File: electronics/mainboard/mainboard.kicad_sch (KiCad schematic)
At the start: 2 parts, among them J1 Conn_02x03_Row_Letter_First

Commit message: add terminals
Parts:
- removed J1: Conn_02x03_Row_Letter_First, symbol Connector_Generic:Conn_02x03_Row_Letter_First
- added J1, J2: Conn_01x09, Wuerth:691247510009, symbol Connector_Generic:Conn_01x09
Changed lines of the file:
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@@
     (pin "VIN")
   )
-  (symbol (lib_id "Connector_Generic:Conn_02x03_Row_Letter_First") (at 100.33 50.8 0) (unit 1)
+  (symbol (lib_id "Connector_Generic:Conn_01x09") (at 71.12 50.8 0) (unit 1)
     (in_bom yes) (on_board yes) (fields_autoplaced)
-    (property "Reference" "J1" (id 0) (at 101.6 41.91 0))
-    (property "Value" "Conn_02x03_Row_Letter_First" (id 1) (at 101.6 44.45 0))
-    (property "Footprint" "" (id 2) (at 100.33 50.8 0)
+    (property "Reference" "J1" (id 0) (at 73.66 49.5299 0)
+      (effects (font (size 1.27 1.27)) (justify left))
+    )
+    (property "Value" "Conn_01x09" (id 1) (at 73.66 52.0699 0)
+      (effects (font (size 1.27 1.27)) (justify left) hide)
+    )
+    (property "Footprint" "Wuerth:691247510009" (id 2) (at 71.12 50.8 0)
       (effects (font (size 1.27 1.27)) hide)
     )
-    (property "Datasheet" "~" (id 3) (at 100.33 50.8 0)
+    (property "Datasheet" "~" (id 3) (at 71.12 50.8 0)
       (effects (font (size 1.27 1.27)) hide)
     )
-    (pin "a1")
-    (pin "a2")
-    (pin "a3")
-    (pin "b1")
-    (pin "b2")
-    (pin "b3")
+    (pin "1")
+    (pin "2")
+    (pin "3")
+    (pin "4")
+    (pin "5")
+    (pin "6")
+    (pin "7")
+    (pin "8")
+    (pin "9")
+  )
+  (symbol (lib_id "Connector_Generic:Conn_01x09") (at 96.52 50.8 0) (unit 1)
+    (in_bom yes) (on_board yes) (fields_autoplaced)
+    (property "Reference" "J2" (id 0) (at 99.06 49.5299 0)
+      (effects (font (size 1.27 1.27)) (justify left))
+    )
+    (property "Value" "Conn_01x09" (id 1) (at 99.06 52.0699 0)
+      (effects (font (size 1.27 1.27)) (justify left) hide)
+    )
+    (property "Footprint" "Wuerth:691247510009" (id 2) (at 96.52 50.8 0)
+      (effects (font (size 1.27 1.27)) hide)
+    )
+    (property "Datasheet" "~" (id 3) (at 96.52 50.8 0)
+      (effects (font (size 1.27 1.27)) hide)
+    )
+    (pin "1")
+    (pin "2")
+    (pin "3")
+    (pin "4")
+    (pin "5")
+    (pin "6")
+    (pin "7")
+    (pin "8")
+    (pin "9")
   )
   (sheet_instances
@@
   )
   (symbol_instances
-    (path "/b954af0c-d64a-4750-8531-d504b8da04e4"
-      (reference "J1") (unit 1) (value "Conn_02x03_Row_Letter_First") (footprint "")
+    (path "/348d43a5-aba5-4633-9cec-22de12d03f26"
+      (reference "J1") (unit 1) (value "Conn_01x09") (footprint "Wuerth:691247510009")
+    )
+    (path "/adc82490-344e-430a-b2ea-febe9c558b97"
+      (reference "J2") (unit 1) (value "Conn_01x09") (footprint "Wuerth:691247510009")
     )
     (path "/135780b7-b5c1-44d5-9cc5-e01fba31ba00"

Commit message: place parts
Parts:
- added J3, J4, J5, J6, J7, J8, J9: Conn_01x09, Wuerth:691247510009, symbol Connector_Generic:Conn_01x09
- added J99: Conn_01x08, Connector_PinHeader_2.54mm:PinHeader_1x08_P2.54mm_Vertical_SMD_Pin1Right, symbol Connector_Generic:Conn_01x08
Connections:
- net at XA1.A0: now also J99.1 (Pin_1)
- net at XA1.A1: now also J99.2 (Pin_2)
- net at XA1.A2: now also J99.3 (Pin_3)
- net at XA1.A3: now also J99.4 (Pin_4)
- net at XA1.A4: now also J99.5 (Pin_5)
- net at XA1.A5: now also J99.6 (Pin_6)
- net at XA1.A6: now also J99.7 (Pin_7)
- net at XA1.A7: now also J99.8 (Pin_8)
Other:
- moved on the sheet: J1, J2

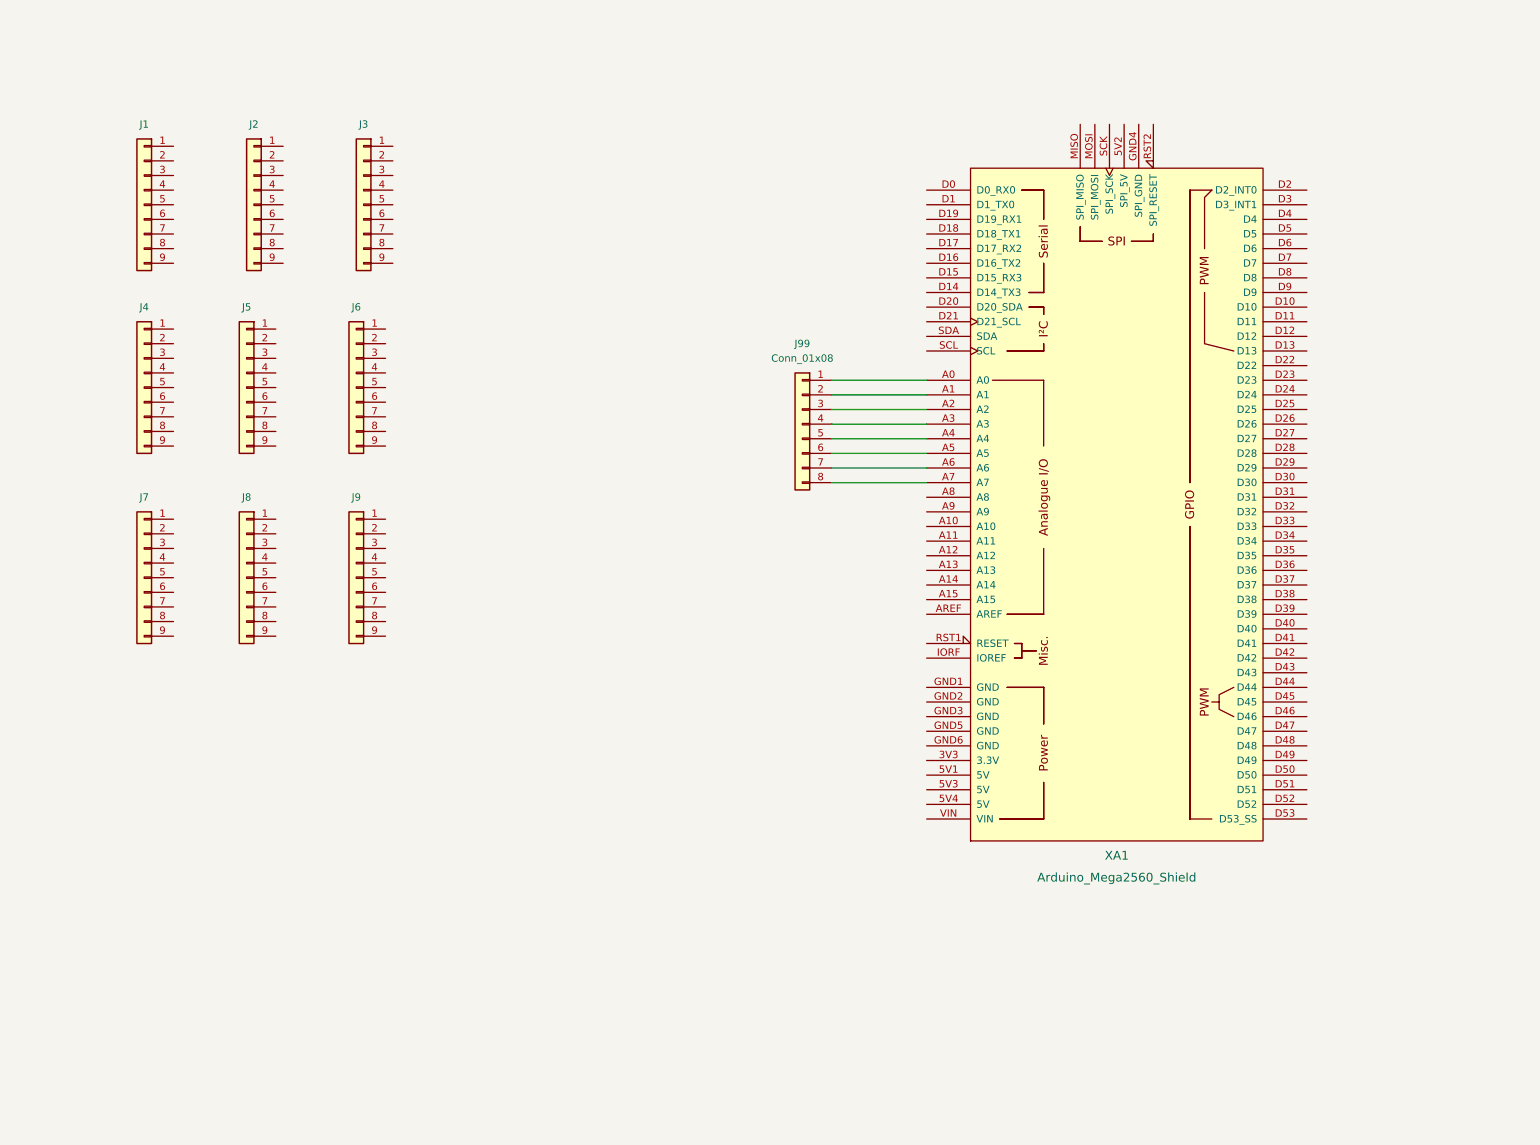
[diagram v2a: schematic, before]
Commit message: add and wire parts in schematic
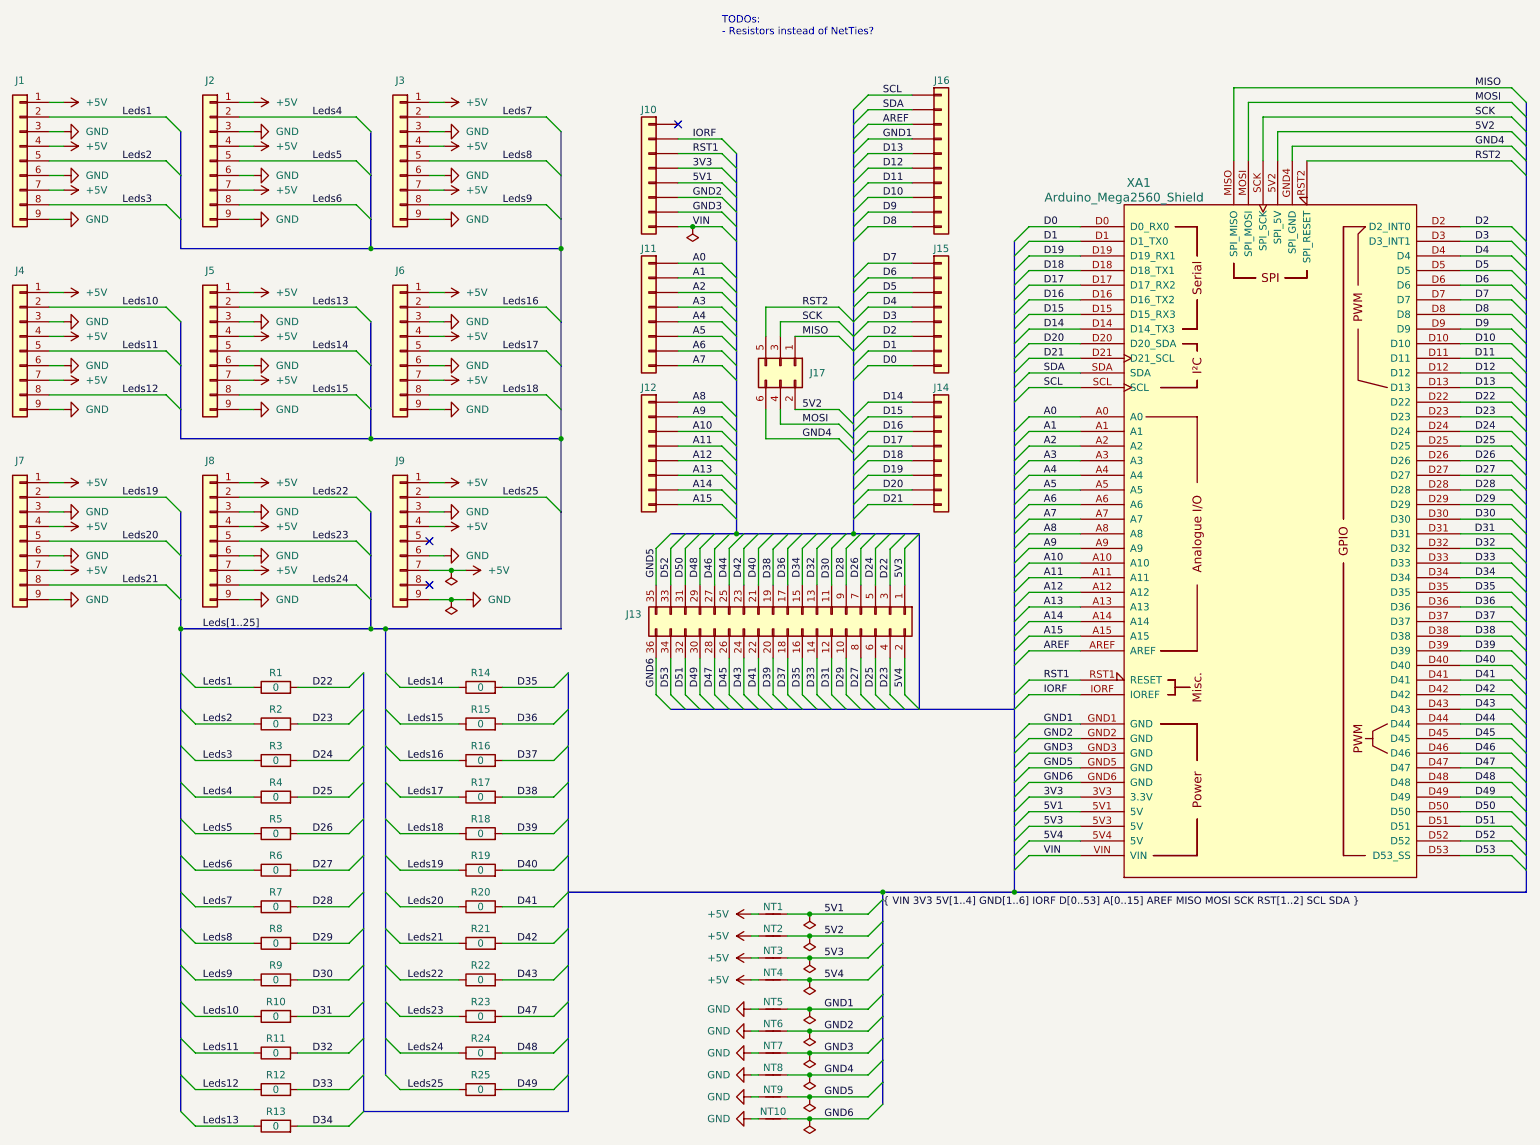
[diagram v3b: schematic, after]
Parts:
- added J10, J11, J12, J14: Conn_01x08, Connector_PinHeader_2.54mm:PinHeader_1x08_P2.54mm_Vertical_SMD_Pin1Right, symbol Connector_Generic:Conn_01x08
- added J13: Conn_02x18_Odd_Even, Connector_PinHeader_2.54mm:PinHeader_2x18_P2.54mm_Vertical_SMD, symbol Connector_Generic:Conn_02x18_Odd_Even
- added J16: Conn_01x10, Connector_PinHeader_2.54mm:PinHeader_1x10_P2.54mm_Vertical_SMD_Pin1Right, symbol Connector_Generic:Conn_01x10
- added J17: Conn_02x03_Odd_Even, Connector_PinHeader_2.54mm:PinHeader_2x03_P2.54mm_Vertical_SMD, symbol Connector_Generic:Conn_02x03_Odd_Even
- added NT1, NT10, NT2, NT3, NT4, NT5, NT6, NT7, NT8, NT9: NetTie_2, NetTie:NetTie-2_SMD_Pad0.5mm, symbol Device:NetTie_2
- added R1, R10, R11, R12, R13, R14, R15, R16, R17, R18, R19, R2, R20, R21, R22, R23, R24, R25, R3, R4, R5, R6, R7, R8, R9: 0, Resistor_SMD:R_0805_2012Metric, symbol Device:R
- renumbered J99 to J15
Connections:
- net 3V3: now reaches XA1.3V3 (3.3V)
- net 3V3: now also J10.4 (Pin_4)
- net 5V1: now reaches XA1.5V1 (5V)
- net 5V1: now also J10.5 (Pin_5), NT1.2
- net 5V2: now reaches XA1.5V2 (SPI_5V)
- net 5V2: now also J17.2 (Pin_2), NT2.2
- net 5V3: now reaches XA1.5V3 (5V)
- net 5V3: now also J13.1 (Pin_1), NT3.2
- net 5V4: now reaches XA1.5V4 (5V)
- net 5V4: now also J13.2 (Pin_2), NT4.2
- net A0: now reaches XA1.A0
- net A0: now also J11.1 (Pin_1); no longer J15.1 (Pin_1)
- net A1: now reaches XA1.A1
- net A1: now also J11.2 (Pin_2); no longer J15.2 (Pin_2)
- net A10: now reaches XA1.A10
- net A10: now also J12.3 (Pin_3)
- net A11: now reaches XA1.A11
- net A11: now also J12.4 (Pin_4)
- net A12: now reaches XA1.A12
- net A12: now also J12.5 (Pin_5)
- net A13: now reaches XA1.A13
- net A13: now also J12.6 (Pin_6)
- net A14: now reaches XA1.A14
- net A14: now also J12.7 (Pin_7)
- net A15: now reaches XA1.A15
- net A15: now also J12.8 (Pin_8)
- net A2: now reaches XA1.A2
- net A2: now also J11.3 (Pin_3); no longer J15.3 (Pin_3)
- net A3: now reaches XA1.A3
- net A3: now also J11.4 (Pin_4); no longer J15.4 (Pin_4)
- net A4: now reaches XA1.A4
- net A4: now also J11.5 (Pin_5); no longer J15.5 (Pin_5)
- net A5: now reaches XA1.A5
- net A5: now also J11.6 (Pin_6); no longer J15.6 (Pin_6)
- net A6: now reaches XA1.A6
- net A6: now also J11.7 (Pin_7); no longer J15.7 (Pin_7)
- net A7: now reaches XA1.A7
- net A7: now also J11.8 (Pin_8); no longer J15.8 (Pin_8)
- net A8: now reaches XA1.A8
- net A8: now also J12.1 (Pin_1)
- net A9: now reaches XA1.A9
- net A9: now also J12.2 (Pin_2)
- net AREF: now reaches XA1.AREF
- net AREF: now also J16.3 (Pin_3)
- net D0: now reaches XA1.D0 (D0_RX0)
- net D0: now also J15.8 (Pin_8)
- net D1: now reaches XA1.D1 (D1_TX0)
- net D1: now also J15.7 (Pin_7)
- net D10: now reaches XA1.D10
- net D10: now also J16.8 (Pin_8)
- net D11: now reaches XA1.D11
- net D11: now also J16.7 (Pin_7)
- net D12: now reaches XA1.D12
- net D12: now also J16.6 (Pin_6)
- net D13: now reaches XA1.D13
- net D13: now also J16.5 (Pin_5)
- net D14: now reaches XA1.D14 (D14_TX3)
- net D14: now also J14.1 (Pin_1)
- net D15: now reaches XA1.D15 (D15_RX3)
- net D15: now also J14.2 (Pin_2)
- net D16: now reaches XA1.D16 (D16_TX2)
- net D16: now also J14.3 (Pin_3)
- net D17: now reaches XA1.D17 (D17_RX2)
- net D17: now also J14.4 (Pin_4)
- net D18: now reaches XA1.D18 (D18_TX1)
- net D18: now also J14.5 (Pin_5)
- net D19: now reaches XA1.D19 (D19_RX1)
- net D19: now also J14.6 (Pin_6)
- net D2: now reaches XA1.D2 (D2_INT0)
- net D2: now also J15.6 (Pin_6)
- net D20: now reaches XA1.D20 (D20_SDA)
- net D20: now also J14.7 (Pin_7)
- net D21: now reaches XA1.D21 (D21_SCL)
- net D21: now also J14.8 (Pin_8)
- net D22: now reaches XA1.D22
- net D22: now also J13.3 (Pin_3), R1.2
- net D23: now reaches XA1.D23
- net D23: now also J13.4 (Pin_4), R2.2
- net D24: now reaches XA1.D24
- net D24: now also J13.5 (Pin_5), R3.2
- net D25: now reaches XA1.D25
- net D25: now also J13.6 (Pin_6), R4.2
- net D26: now reaches XA1.D26
- net D26: now also J13.7 (Pin_7), R5.2
- net D27: now reaches XA1.D27
- net D27: now also J13.8 (Pin_8), R6.2
- net D28: now reaches XA1.D28
- net D28: now also J13.9 (Pin_9), R7.2
- net D29: now reaches XA1.D29
- net D29: now also J13.10 (Pin_10), R8.2
- net D3: now reaches XA1.D3 (D3_INT1)
- net D3: now also J15.5 (Pin_5)
- net D30: now reaches XA1.D30
- net D30: now also J13.11 (Pin_11), R9.2
- net D31: now reaches XA1.D31
- net D31: now also J13.12 (Pin_12), R10.2
- net D32: now reaches XA1.D32
- net D32: now also J13.13 (Pin_13), R11.2
- net D33: now reaches XA1.D33
- net D33: now also J13.14 (Pin_14), R12.2
- net D34: now reaches XA1.D34
- net D34: now also J13.15 (Pin_15), R13.2
- net D35: now reaches XA1.D35
- net D35: now also J13.16 (Pin_16), R14.2
- net D36: now reaches XA1.D36
- net D36: now also J13.17 (Pin_17), R15.2
- net D37: now reaches XA1.D37
- net D37: now also J13.18 (Pin_18), R16.2
- net D38: now reaches XA1.D38
- net D38: now also J13.19 (Pin_19), R17.2
- net D39: now reaches XA1.D39
- net D39: now also J13.20 (Pin_20), R18.2
- net D4: now reaches XA1.D4
- net D4: now also J15.4 (Pin_4)
- net D40: now reaches XA1.D40
- net D40: now also J13.21 (Pin_21), R19.2
- net D41: now reaches XA1.D41
- net D41: now also J13.22 (Pin_22), R20.2
- net D42: now reaches XA1.D42
- net D42: now also J13.23 (Pin_23), R21.2
- net D43: now reaches XA1.D43
- net D43: now also J13.24 (Pin_24), R22.2
- net D44: now reaches XA1.D44
- net D44: now also J13.25 (Pin_25)
- net D45: now reaches XA1.D45
- net D45: now also J13.26 (Pin_26)
- net D46: now reaches XA1.D46
- net D46: now also J13.27 (Pin_27)
- net D47: now reaches XA1.D47
- net D47: now also J13.28 (Pin_28), R23.2
- net D48: now reaches XA1.D48
- net D48: now also J13.29 (Pin_29), R24.2
- net D49: now reaches XA1.D49
- net D49: now also J13.30 (Pin_30), R25.2
- net D5: now reaches XA1.D5
- net D5: now also J15.3 (Pin_3)
- net D50: now reaches XA1.D50
- net D50: now also J13.31 (Pin_31)
- net D51: now reaches XA1.D51
- net D51: now also J13.32 (Pin_32)
- net D52: now reaches XA1.D52
- net D52: now also J13.33 (Pin_33)
- net D53: now reaches XA1.D53 (D53_SS)
- net D53: now also J13.34 (Pin_34)
- net D6: now reaches XA1.D6
- net D6: now also J15.2 (Pin_2)
- net D7: now reaches XA1.D7
- net D7: now also J15.1 (Pin_1)
- net D8: now reaches XA1.D8
- net D8: now also J16.10 (Pin_10)
- net D9: now reaches XA1.D9
- net D9: now also J16.9 (Pin_9)
- net GND1: now reaches XA1.GND1 (GND)
- net GND1: now also J16.4 (Pin_4), NT5.2
- net GND2: now reaches XA1.GND2 (GND)
- net GND2: now also J10.6 (Pin_6), NT6.2
- net GND3: now reaches XA1.GND3 (GND)
- net GND3: now also J10.7 (Pin_7), NT7.2
- net GND4: now reaches XA1.GND4 (SPI_GND)
- net GND4: now also J17.6 (Pin_6), NT8.2
- net GND5: now reaches XA1.GND5 (GND)
- net GND5: now also J13.35 (Pin_35), NT9.2
- net GND6: now reaches XA1.GND6 (GND)
- net GND6: now also J13.36 (Pin_36), NT10.2
- net IORF: now reaches XA1.IORF (IOREF)
- net IORF: now also J10.2 (Pin_2)
- net MISO: now reaches XA1.MISO (SPI_MISO)
- net MISO: now also J17.1 (Pin_1)
- net MOSI: now reaches XA1.MOSI (SPI_MOSI)
- net MOSI: now also J17.4 (Pin_4)
- net RST1: now reaches XA1.RST1 (RESET)
- net RST1: now also J10.3 (Pin_3)
- net RST2: now reaches XA1.RST2 (SPI_RESET)
- net RST2: now also J17.5 (Pin_5)
- net SCK: now reaches XA1.SCK (SPI_SCK)
- net SCK: now also J17.3 (Pin_3)
- net SCL: now reaches XA1.SCL
- net SCL: now also J16.1 (Pin_1)
- net SDA: now reaches XA1.SDA
- net SDA: now also J16.2 (Pin_2)
- net VIN: now reaches XA1.VIN
- net VIN: now also J10.8 (Pin_8)
- net +5V: now reaches J5.1 (Pin_1)
- net +5V: now also J1.1 (Pin_1), J1.4 (Pin_4), J1.7 (Pin_7), J2.1 (Pin_1), J2.4 (Pin_4), J2.7 (Pin_7), J3.1 (Pin_1), J3.4 (Pin_4), J3.7 (Pin_7), J4.1 (Pin_1), J4.4 (Pin_4), J4.7 (Pin_7), J5.4 (Pin_4), J5.7 (Pin_7), J6.1 (Pin_1), J6.4 (Pin_4), J6.7 (Pin_7), J7.1 (Pin_1), J7.4 (Pin_4), J7.7 (Pin_7), J8.1 (Pin_1), J8.4 (Pin_4), J8.7 (Pin_7), J9.1 (Pin_1), J9.4 (Pin_4), J9.7 (Pin_7), NT1.1, NT2.1, NT3.1, NT4.1
- net Leds13: now reaches J5.2 (Pin_2)
- net Leds13: now also R13.1
- net GND: now reaches J5.3 (Pin_3)
- net GND: now also J1.3 (Pin_3), J1.6 (Pin_6), J1.9 (Pin_9), J2.3 (Pin_3), J2.6 (Pin_6), J2.9 (Pin_9), J3.3 (Pin_3), J3.6 (Pin_6), J3.9 (Pin_9), J4.3 (Pin_3), J4.6 (Pin_6), J4.9 (Pin_9), J5.6 (Pin_6), J5.9 (Pin_9), J6.3 (Pin_3), J6.6 (Pin_6), J6.9 (Pin_9), J7.3 (Pin_3), J7.6 (Pin_6), J7.9 (Pin_9), J8.3 (Pin_3), J8.6 (Pin_6), J8.9 (Pin_9), J9.3 (Pin_3), J9.6 (Pin_6), J9.9 (Pin_9), NT10.1, NT5.1, NT6.1, NT7.1, NT8.1, NT9.1
- net Leds14: now reaches J5.5 (Pin_5)
- net Leds14: now also R14.1
- net Leds15: now reaches J5.8 (Pin_8)
- net Leds15: now also R15.1
- net Leds1: now reaches J1.2 (Pin_2)
- net Leds1: now also R1.1
- net Leds2: now reaches J1.5 (Pin_5)
- net Leds2: now also R2.1
- net Leds3: now reaches J1.8 (Pin_8)
- net Leds3: now also R3.1
- net Leds25: now reaches J9.2 (Pin_2)
- net Leds25: now also R25.1
- net Leds16: now reaches J6.2 (Pin_2)
- net Leds16: now also R16.1
- net Leds17: now reaches J6.5 (Pin_5)
- net Leds17: now also R17.1
- net Leds18: now reaches J6.8 (Pin_8)
- net Leds18: now also R18.1
- net Leds22: now reaches J8.2 (Pin_2)
- net Leds22: now also R22.1
- net Leds23: now reaches J8.5 (Pin_5)
- net Leds23: now also R23.1
- net Leds24: now reaches J8.8 (Pin_8)
- net Leds24: now also R24.1
- net Leds10: now reaches J4.2 (Pin_2)
- net Leds10: now also R10.1
- net Leds11: now reaches J4.5 (Pin_5)
- net Leds11: now also R11.1
- net Leds12: now reaches J4.8 (Pin_8)
- net Leds12: now also R12.1
- net Leds19: now reaches J7.2 (Pin_2)
- net Leds19: now also R19.1
- net Leds20: now reaches J7.5 (Pin_5)
- net Leds20: now also R20.1
- net Leds21: now reaches J7.8 (Pin_8)
- net Leds21: now also R21.1
- net Leds4: now reaches J2.2 (Pin_2)
- net Leds4: now also R4.1
- net Leds5: now reaches J2.5 (Pin_5)
- net Leds5: now also R5.1
- net Leds6: now reaches J2.8 (Pin_8)
- net Leds6: now also R6.1
- net Leds7: now reaches J3.2 (Pin_2)
- net Leds7: now also R7.1
- net Leds8: now reaches J3.5 (Pin_5)
- net Leds8: now also R8.1
- net Leds9: now reaches J3.8 (Pin_8)
- net Leds9: now also R9.1
- no-connect marks 0 -> 3
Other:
- note added: "TODOs: - Resistors instead of NetTies?"
- moved on the sheet: J1, J2, J3, J4, J5, J6, J7, J8, J9, XA1
